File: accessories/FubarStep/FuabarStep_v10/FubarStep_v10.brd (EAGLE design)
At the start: 71.1 x 85.7 mm, 10 parts, among them IC1 7805, X1 DC21MMX

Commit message: More work.
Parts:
- removed AD: (no value), pinhead:1X06
- removed IOL, POWER: (no value), pinhead:1X08
- added C10, C11, C12, C13, C14, C15, C18, C19, C8, C9: .1uF, SparkFun-Capacitors:CAP-PTH-SMALL
- added C16, C17, C5: 100uF, SparkFun-Capacitors:CPOL-RADIAL-100UF-25V
- added IC2, IC3: SN754410NE, texas:DIL16
- added JP10, JP11, JP12, JP13, JP14, JP15, JP16, JP17, JP18, JP19, JP20, JP21, JP22, JP23, JP24, JP25, JP26, JP27, JP3, JP4, JP5, JP6: (no value), SparkFun-Connectors:1X03_LOCK
- added JP2: (no value), SparkFun-Connectors:SCREWTERMINAL-3.5MM-4_LOCK
- added JP7, JP8, JP9: (no value), SparkFun-Connectors:1X04_LOCK
- added LOGO1: OSHW-LOGOM, SparkFun-Aesthetics:OSHW-LOGO-M
- C2: value 10uF -> 100uF; device SparkFun-Capacitors:CPOL-RADIAL-10UF-25V -> SparkFun-Capacitors:CPOL-RADIAL-100UF-25V
- IC1: value 7805 -> OKI-78SR-5/1.5-W36H-C
- JP1: device pinhead:1X10 -> SparkFun-Connectors:SCREWTERMINAL-3.5MM-4_LOCK
- moved JP1 47.7 mm to (47.6, 6.35), turned to 0 degrees
- moved C1 32.2 mm to (27.9, 44.5), turned to 180 degrees
- moved C2 28.7 mm to (17.8, 43.8), turned to 180 degrees
- moved X1 14.2 mm to (19.6, 9.14), turned to 180 degrees
- moved IC1 10.0 mm to (15.2, 35.6), turned to 90 degrees
- moved U$1 6.98 mm to (35.6, 61.0)
- moved U$2 6.98 mm to (25.4, 61.0)
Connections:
- removed net AD0: AD.1
- removed net AD1: AD.2
- removed net AD2: AD.3
- removed net AD3: AD.4
- removed net AD4: AD.5
- removed net AD4/SDA: JP1.9
- removed net AD5: AD.6
- removed net AD5/SCL: JP1.10
- removed net AREF: JP1.8
- removed net IO0: IOL.1
- removed net IO1: IOL.2
- removed net IO2: IOL.3
- removed net IO3: IOL.4
- removed net IO4: IOL.5
- removed net IO5: IOL.6
- removed net IO6: IOL.7
- removed net IO7: IOL.8
- removed net IO8: JP1.1
- removed net IO9: JP1.2
- removed net MISO: JP1.5
- removed net MOSI: JP1.4
- removed net SCK: JP1.6
- removed net SS: JP1.3
- new net M1A1: IC2.2
- new net M1A2: IC2.7
- new net M1A3: IC2.10
- new net M1A4: IC2.15
- new net M1EN12: IC2.1, U$1.11
- new net M1EN34: IC2.9, U$1.12
- new net M1O1: C10.2, IC2.3, JP1.1
- new net M1O2: C11.2, IC2.6, JP1.2
- new net M1O3: C12.1, IC2.11, JP1.3
- new net M1O4: C9.1, IC2.14, JP1.4
- new net M2A1: IC3.2
- new net M2A2: IC3.7
- new net M2A3: IC3.10
- new net M2A4: IC3.15
- new net M2EN12: IC3.1, U$1.13
- new net M2EN34: IC3.9, U$1.14
- new net M2O1: C8.2, IC3.3, JP2.1
- new net M2O2: C13.2, IC3.6, JP2.2
- new net M2O3: C15.1, IC3.11, JP2.3
- new net M2O4: C14.1, IC3.14, JP2.4
- new net N$12: JP8.1
- new net N$2: JP18.1
- new net N$29: JP9.1
- new net N$3: JP19.1
- new net N$67: JP9.2
- new net N$68: JP9.3
- new net N$69: JP23.1
- new net N$87: JP22.1
- new net N$88: JP17.1
- new net N$89: JP16.1
- new net N$90: JP15.1
- new net N$91: JP14.1
- new net N$92: JP10.1
- new net N$93: JP11.1
- new net N$94: JP12.1
- new net N$95: JP13.1
- new net N$96: JP24.1
- new net N$97: JP25.1
- new net RX: JP7.3, U$1.52
- new net SERVO1: JP6.1
- new net SERVO2: JP3.1
- new net SERVO3: JP4.1
- new net SERVO4: JP5.1
- new net TX: JP7.2, U$1.53
- net +3V3: no longer POWER.4
- net +5V: now also C18.1, C19.1, C5.1, IC2.16, IC3.16, JP10.2, JP11.2, JP12.2, JP13.2, JP14.2, JP15.2, JP16.2, JP17.2, JP18.2, JP19.2, JP20.2, JP21.2, JP22.2, JP23.2, JP24.2, JP25.2, JP26.2, JP27.2, JP3.2, JP4.2, JP5.2, JP6.2, JP7.1, U$1.56, U$2.40; no longer POWER.2, POWER.5, U$1.1, U$2.1
- net GND: now also C10.1, C11.1, C12.2, C13.1, C14.2, C15.2, C16.2, C17.2, C18.2, C19.2, C5.2, C8.1, C9.2, IC2.12, IC2.13, IC2.4, IC2.5, IC3.12, IC3.13, IC3.4, IC3.5, JP10.3, JP11.3, JP12.3, JP13.3, JP14.3, JP15.3, JP16.3, JP17.3, JP18.3, JP19.3, JP20.3, JP21.3, JP22.3, JP23.3, JP24.3, JP25.3, JP26.3, JP27.3, JP3.3, JP4.3, JP5.3, JP6.3, JP7.4, JP8.4, JP9.4; no longer JP1.7, POWER.6, POWER.7
- net N$11: now also JP20.1; no longer U$1.11
- net N$13: now also JP8.2; no longer U$1.12
- net N$14: now also JP8.3; no longer U$1.13
- net N$15: now also JP21.1; no longer U$1.14
- net N$33: now also JP26.1; no longer U$1.53
- net N$34: now also JP27.1; no longer U$1.52
- net RESET: no longer POWER.3
- net VIN: now also C16.1, C17.1, IC2.8, IC3.8; no longer POWER.8, U$1.56, U$2.40
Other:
- board size 71.1 x 85.7 mm -> 71.1 x 83.8 mm
- board text removed: "#"
- board text removed: "0"
- board text removed: "1"
- board text removed: "10"
- board text removed: "11"
- board text removed: "12"
- board text removed: "13"
- board text removed: "2"
- board text removed: "3"
- board text removed: "3V3"
- board text removed: "4"
- board text removed: "5"
- board text removed: "5V"
- board text removed: "6"
- board text removed: "7"
- board text removed: "8"
- board text removed: "9"
- board text removed: "A0"
- board text removed: "A1"
- board text removed: "A2"
- board text removed: "A3"
- board text removed: "A4"
- board text removed: "A5"
- board text removed: "ANALOG IN"
- board text removed: "AREF"
- board text removed: "DIGITAL"
- board text removed: "GND"
- board text removed: "RESET"
- board text removed: "RX"
- board text removed: "TX"
- board text removed: "VIN"
- board text removed: "[#=PWM]"

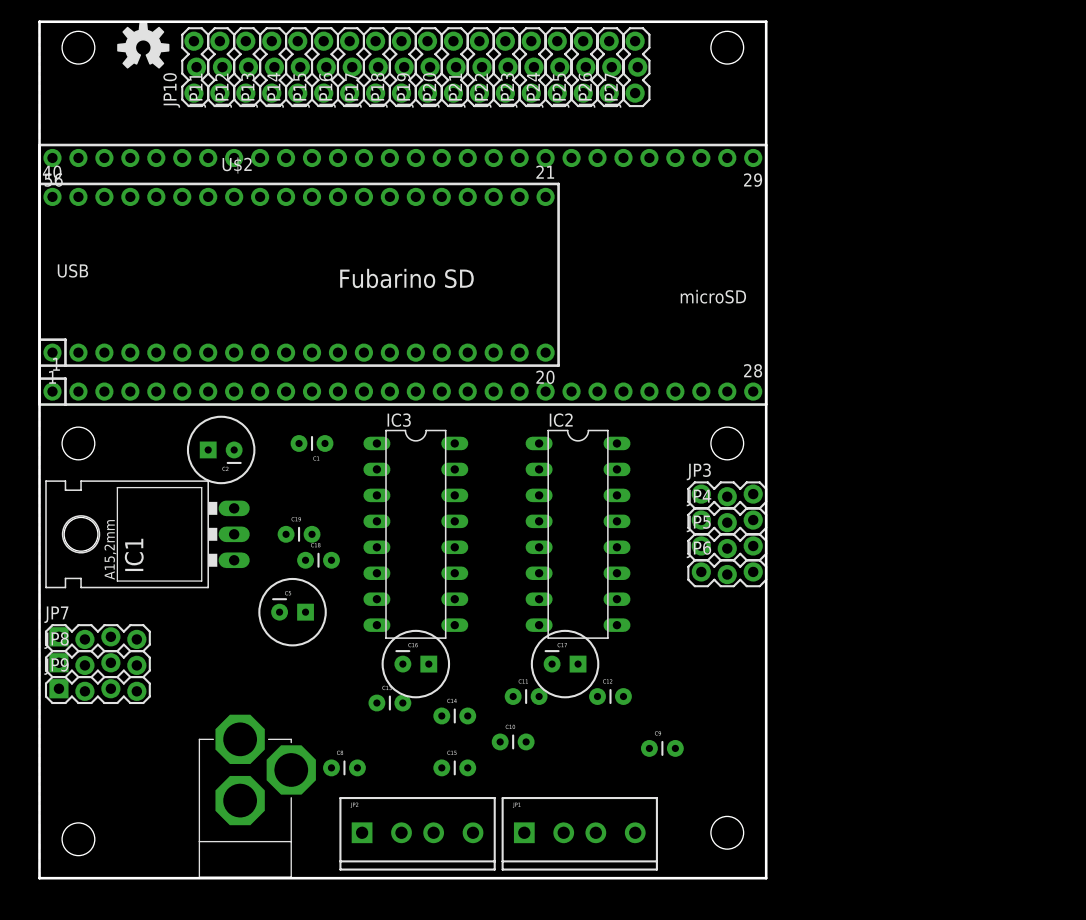
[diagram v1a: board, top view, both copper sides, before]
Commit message: Renamed board from thin to normal, added all Mini routing except for 2 pins (maybe TX/RX?) Almost done!
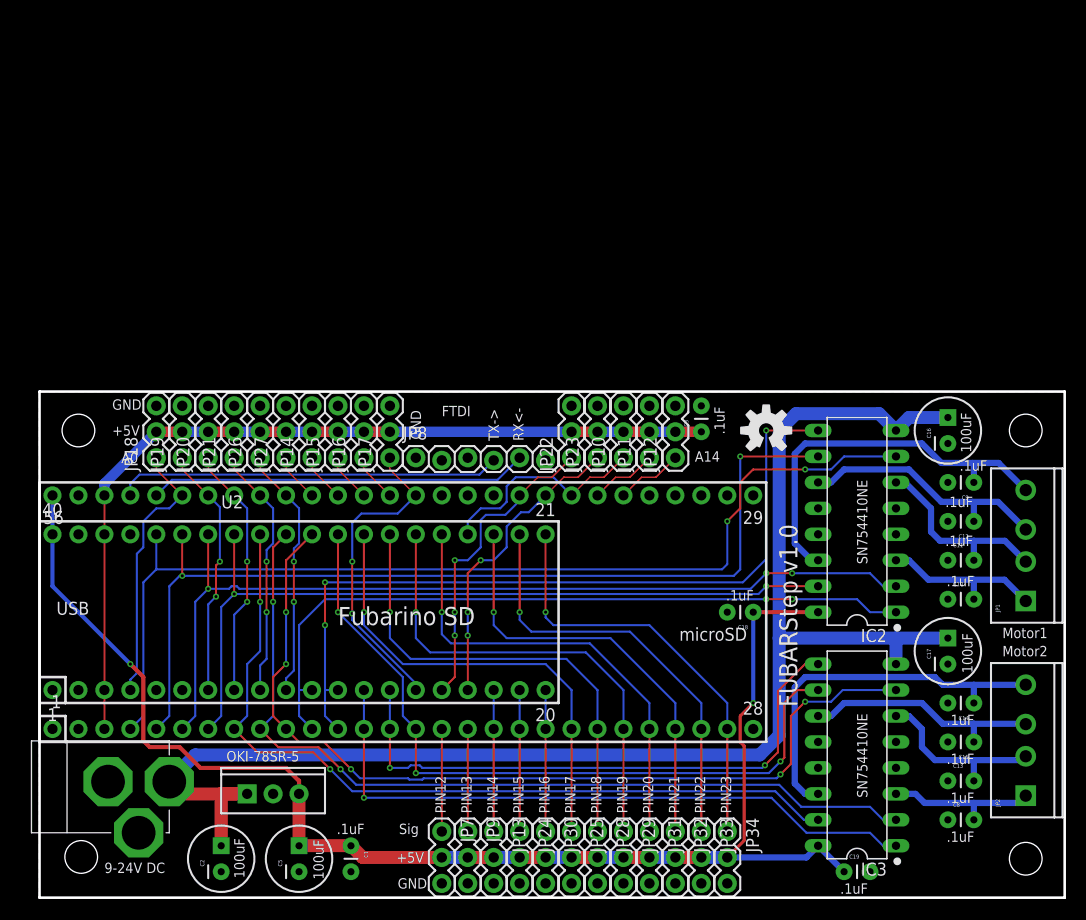
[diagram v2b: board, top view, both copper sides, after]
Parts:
- removed IC1: OKI-78SR-5/1.5-W36H-C, SparkFun-PowerIC:78XXL
- removed JP3, JP4, JP5, JP6: (no value), SparkFun-Connectors:1X03_LOCK
- removed U$1: FUBARINO_SD, SchmalzHausPublic:FUBARINO_SD
- removed U$2: FUBARINO_MINI, SchmalzHausPublic:FUBARINO_MINI
- added C3: .1uF, SparkFun-Capacitors:CAP-PTH-SMALL
- added JP28, JP29, JP30, JP31, JP32, JP33, JP34: (no value), SparkFun-Connectors:1X03
- added U1: FUBARINO_SD, SchmalzHausPublic:FUBARINO_SD
- added U2: FUBARINO_MINI, SchmalzHausPublic:FUBARINO_MINI
- added U3: OKI-78SR-5/1.5-W36H-C, SparkFun-PowerIC:TO220-IGO
- JP10, JP11, JP12, JP13, JP14, JP15, JP16, JP17, JP18, JP19, JP20, JP21, JP22, JP23, JP24, JP25, JP26, JP27: device SparkFun-Connectors:1X03_LOCK -> SparkFun-Connectors:1X03
- JP7, JP9: device SparkFun-Connectors:1X04_LOCK -> SparkFun-Connectors:1X03
- JP8: device SparkFun-Connectors:1X04_LOCK -> SparkFun-Connectors:1X06_LOCK
- moved JP13 75.4 mm to (44.5, 6.48), turned to 270 degrees
- moved JP24 72.4 mm to (47.0, 6.48), turned to 270 degrees
- moved JP25 72.3 mm to (52.1, 6.48), turned to 270 degrees
- moved LOGO1 71.6 mm to (71.1, 45.7)
- moved JP2 64.9 mm to (96.5, 10.2), turned to 90 degrees
- moved C19 63.8 mm to (78.7, 2.54)
- moved C8 60.5 mm to (88.9, 7.62)
- moved C16 56.9 mm to (88.9, 45.7), turned to 90 degrees
- moved C13 56.4 mm to (88.9, 11.4)
- moved JP10 55.0 mm to (57.1, 43.1)
- moved JP11 55.0 mm to (59.7, 43.1)
- moved JP12 55.0 mm to (62.2, 43.1)
- moved JP1 54.0 mm to (96.5, 29.2), turned to 90 degrees
- moved C15 52.1 mm to (91.4, 15.2), turned to 180 degrees
- moved C14 52.1 mm to (91.4, 19.1), turned to 180 degrees
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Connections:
- removed net N$10: U$1.10
- removed net N$11: JP20.1
- removed net N$12: JP8.1
- removed net N$13: JP8.2
- removed net N$14: JP8.3
- removed net N$15: JP21.1
- removed net N$16: U$1.15
- removed net N$17: U$1.16
- removed net N$18: U$1.17
- removed net N$19: U$1.18
- removed net N$2: JP18.1
- removed net N$20: U$1.19
- removed net N$21: U$1.20
- removed net N$22: U$1.21
- removed net N$23: U$1.22
- removed net N$24: U$1.23
- removed net N$25: U$1.24
- removed net N$26: U$1.25
- removed net N$27: U$1.26
- removed net N$28: U$1.27
- removed net N$29: JP9.1
- removed net N$3: JP19.1
- removed net N$30: U$2.36
- removed net N$31: U$2.35
- removed net N$32: U$2.34
- removed net N$33: JP26.1
- removed net N$34: JP27.1
- removed net N$35: U$1.51
- removed net N$36: U$1.50
- removed net N$37: U$1.49
- removed net N$38: U$1.48
- removed net N$39: U$1.47
- removed net N$4: U$1.4
- removed net N$40: U$1.46
- removed net N$41: U$1.45
- removed net N$42: U$1.44
- removed net N$43: U$1.43
- removed net N$44: U$1.42
- removed net N$45: U$2.33
- removed net N$46: U$2.32
- removed net N$47: U$2.31
- removed net N$48: U$1.38
- removed net N$49: U$1.37
- removed net N$5: U$1.5
- removed net N$50: U$1.36
- removed net N$51: U$1.35
- removed net N$52: U$1.34
- removed net N$53: U$1.33
- removed net N$54: U$1.32
- removed net N$55: U$1.31
- removed net N$56: U$1.30
- removed net N$57: U$2.30
- removed net N$58: U$2.29
- removed net N$59: U$2.28
- removed net N$6: U$1.6
- removed net N$60: U$2.27
- removed net N$61: U$2.26
- removed net N$62: U$2.25
- removed net N$63: U$2.24
- removed net N$64: U$2.23
- removed net N$65: U$2.22
- removed net N$66: U$2.21
- removed net N$67: JP9.2
- removed net N$68: JP9.3
- removed net N$69: JP23.1
- removed net N$7: U$1.7
- removed net N$70: U$2.4
- removed net N$71: U$2.5
- removed net N$72: U$2.6
- removed net N$73: U$2.7
- removed net N$74: U$2.8
- removed net N$75: U$2.9
- removed net N$76: U$2.10
- removed net N$77: U$2.11
- removed net N$78: U$2.12
- removed net N$79: U$2.13
- removed net N$8: U$1.8
- removed net N$80: U$2.14
- removed net N$81: U$2.15
- removed net N$82: U$2.16
- removed net N$83: U$2.17
- removed net N$84: U$2.18
- removed net N$85: U$2.19
- removed net N$86: U$2.20
- removed net N$87: JP22.1
- removed net N$88: JP17.1
- removed net N$89: JP16.1
- removed net N$9: U$1.9
- removed net N$90: JP15.1
- removed net N$91: JP14.1
- removed net N$92: JP10.1
- removed net N$93: JP11.1
- removed net N$94: JP12.1
- removed net N$95: JP13.1
- removed net N$96: JP24.1
- removed net N$97: JP25.1
- removed net SERVO1: JP6.1
- removed net SERVO2: JP3.1
- removed net SERVO3: JP4.1
- removed net SERVO4: JP5.1
- new net $01: U2.5
- new net $02: U2.6
- new net 3.3V: C3.1, JP10.2, JP11.2, JP12.2, JP14.2, JP15.2, JP16.2, JP17.2, JP18.2, JP19.2, JP20.2, JP21.2, JP22.2, JP23.2, JP26.2, JP27.2, U1.3, U1.54, U2.3, U2.38
- new net A0: JP18.1, U1.51, U2.4
- new net A1: JP19.1, U1.50, U2.7
- new net A10: JP22.1, U1.38, U2.16
- new net A11: JP23.1, U1.37, U2.17
- new net A12: JP10.1, U1.36, U2.24
- new net A13: JP11.1, U1.35
- new net A14: JP12.1, U1.34
- new net A2: JP20.1, U1.49, U2.8
- new net A3: JP21.1, U1.48, U2.9
- new net A4: JP26.1, U1.47, U2.10
- new net A5: JP27.1, U1.46
- new net A6: JP14.1, U1.45
- new net A7: JP15.1, U1.44
- new net A8: JP16.1, U1.43
- new net A9: JP17.1, U1.42, U2.15
- new net PIN12: JP7.1, U1.16
- new net PIN13: JP9.1, U1.17
- new net PIN14: JP13.1, U1.18, U2.18
- new net PIN15: JP24.1, U1.19, U2.19
- new net PIN16: JP30.1, U1.20, U2.20
- new net PIN17: JP25.1, U1.21, U2.28
- new net PIN18: JP28.1, U1.22, U2.27
- new net PIN19: JP29.1, U1.23, U2.26
- new net PIN20: JP31.1, U1.24, U2.25
- new net PIN21: JP32.1, U1.25, U2.23
- new net PIN22: JP33.1, U1.26, U2.22
- new net PIN23: JP34.1, U1.27, U2.21
- net +3V3: now also U1.40; no longer U$1.3, U$1.40, U$1.54, U$2.3, U$2.38
- net +5V: now also JP28.2, JP29.2, JP30.2, JP31.2, JP32.2, JP33.2, JP34.2, JP7.2, JP9.2, U1.56, U2.40, U3.OUT; no longer IC1.OUT, JP10.2, JP11.2, JP12.2, JP14.2, JP15.2, JP16.2, JP17.2, JP18.2, JP19.2, JP20.2, JP21.2, JP22.2, JP23.2, JP26.2, JP27.2, JP3.2, JP4.2, JP5.2, JP6.2, JP7.1, U$1.56, U$2.40
- net GND: now also C3.2, JP28.3, JP29.3, JP30.3, JP31.3, JP32.3, JP33.3, JP34.3, JP7.3, JP8.1, JP9.3, U1.2, U1.28, U1.29, U1.41, U1.55, U2.2, U2.37, U2.39, U3.GND; no longer IC1.GND, JP3.3, JP4.3, JP5.3, JP6.3, JP7.4, JP8.4, JP9.4, U$1.2, U$1.28, U$1.29, U$1.41, U$1.55, U$2.2, U$2.37, U$2.39
- net M1A1: now also U1.6, U2.34
- net M1A2: now also U1.4, U2.36
- net M1A3: now also U1.5, U2.35
- net M1A4: now also U1.7, U2.33
- net M1EN12: now also U1.11, U2.11; no longer U$1.11
- net M1EN34: now also U1.12, U2.12; no longer U$1.12
- net M2A1: now also U1.9, U2.31
- net M2A2: now also U1.10, U2.30
- net M2A3: now also U1.15, U2.29
- net M2A4: now also U1.8, U2.32
- net M2EN12: now also U1.13, U2.13; no longer U$1.13
- net M2EN34: now also U1.14, U2.14; no longer U$1.14
- net RESET: now also U1.39; no longer U$1.39
- net RX: now also JP8.5, U1.52; no longer JP7.3, U$1.52
- net TX: now also JP8.4, U1.53; no longer JP7.2, U$1.53
- net VIN: now also U3.IN; no longer IC1.IN
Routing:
- net VIN: track 0.00 -> 144.6 mm
- net +5V: track 0.00 -> 138.0 mm, vias 0 -> 2
- net M1A2: track 0.00 -> 101.0 mm, vias 0 -> 2
- net M1A3: track 0.00 -> 93.8 mm, vias 0 -> 2
- net M2A2: track 0.00 -> 89.3 mm, vias 0 -> 5
- net M1A1: track 0.00 -> 88.8 mm, vias 0 -> 3
- net M2A1: track 0.00 -> 86.0 mm, vias 0 -> 2
- net 3.3V: track 0.00 -> 84.5 mm
- net M2A4: track 0.00 -> 80.9 mm, vias 0 -> 2
- net M1EN34: track 0.00 -> 77.9 mm, vias 0 -> 3
- net M1A4: track 0.00 -> 77.6 mm, vias 0 -> 2
- net M2A3: track 0.00 -> 72.4 mm, vias 0 -> 3
- net M1EN12: track 0.00 -> 72.0 mm, vias 0 -> 2
- net M2EN12: track 0.00 -> 64.6 mm, vias 0 -> 1
- net M2EN34: track 0.00 -> 57.4 mm, vias 0 -> 2
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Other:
- board size 71.1 x 83.8 mm -> 100.3 x 49.5 mm
- board text added: "+5V"
- board text added: ".1uF"
- board text added: "100uF"
- board text added: "9-24V DC"
- board text added: "A0"
- board text added: "A14"
- board text added: "ANALOG INPUTS/3.3V GPIO"
- board text added: "FTDI"
- board text added: "FUBARStep v1.0"
- board text added: "GND"
- board text added: "Motor1"
- board text added: "Motor2"
- board text added: "OKI-78SR-5"
- board text added: "PIN12"
- board text added: "PIN13"
- board text added: "PIN14"
- board text added: "PIN15"
- board text added: "PIN16"
- board text added: "PIN17"
- board text added: "PIN18"
- board text added: "PIN19"
- board text added: "PIN20"
- board text added: "PIN21"
- board text added: "PIN22"
- board text added: "PIN23"
- board text added: "RX<-"
- board text added: "SERVO OUTPUTS/5V GPIO"
- board text added: "SN754410NE"
- board text added: "Sig"
- board text added: "TX->"

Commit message: Version 1.0 done - routed, schematic done (with license), just need to add BOM now.
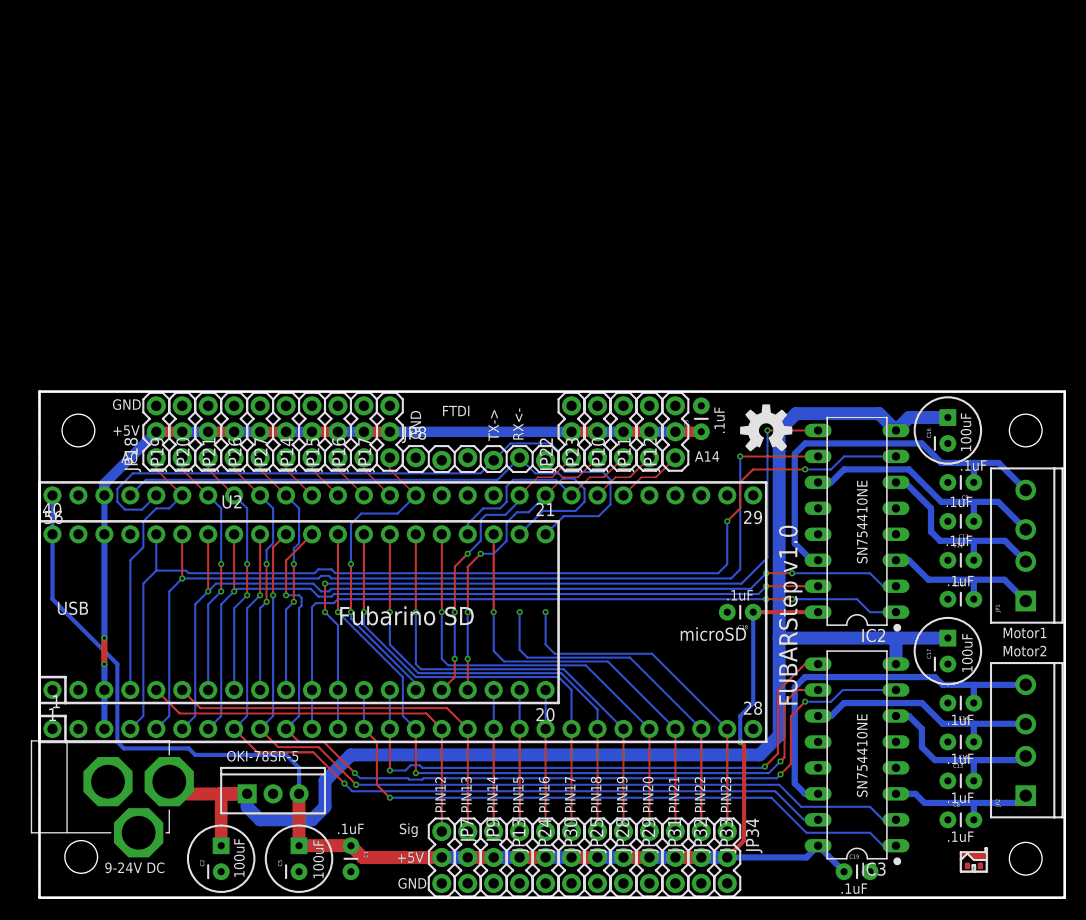
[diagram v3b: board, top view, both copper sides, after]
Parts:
- added U$1: SCHMALZHAUSSCHMALZHAUS_SMALL, SchmalzHaus:SCHMALZHAUS_SMALL
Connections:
- removed net $01: U2.5
- removed net $02: U2.6
- net PIN12: now also U2.5
- net PIN13: now also U2.6
- net PIN22: no longer U2.22
- net PIN23: no longer U2.21
- net RX: now also JP8.4, U2.21; no longer JP8.5
- net TX: now also JP8.5, U2.22; no longer JP8.4
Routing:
- net RX: track 37.1 -> 68.3 mm
- net PIN13: track 10.0 -> 39.6 mm
- net PIN12: track 10.0 -> 39.6 mm
- net TX: track 37.6 -> 56.2 mm
- net PIN23: track 42.0 -> 34.4 mm
- net PIN22: track 42.1 -> 34.7 mm
- net VIN: track 144.6 -> 141.9 mm
- net +5V: track 138.0 -> 140.3 mm, vias 2 -> 1
- net M1EN12: track 72.0 -> 69.9 mm
- net M2EN12: track 64.6 -> 63.1 mm
- net M1EN34: track 77.9 -> 76.5 mm
- net M2A2: track 89.3 -> 90.2 mm, vias 5 -> 4
- net PIN18: track 46.4 -> 45.7 mm
- net PIN19: track 46.4 -> 45.7 mm
- net A10: track 30.7 -> 29.9 mm
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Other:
- board text added: "FUBARStep v1.0 Creatded by FUBARLabs and Schmalz Haus www.fubarlabs.org www.schmalzhaus.com www.fubarino.org"

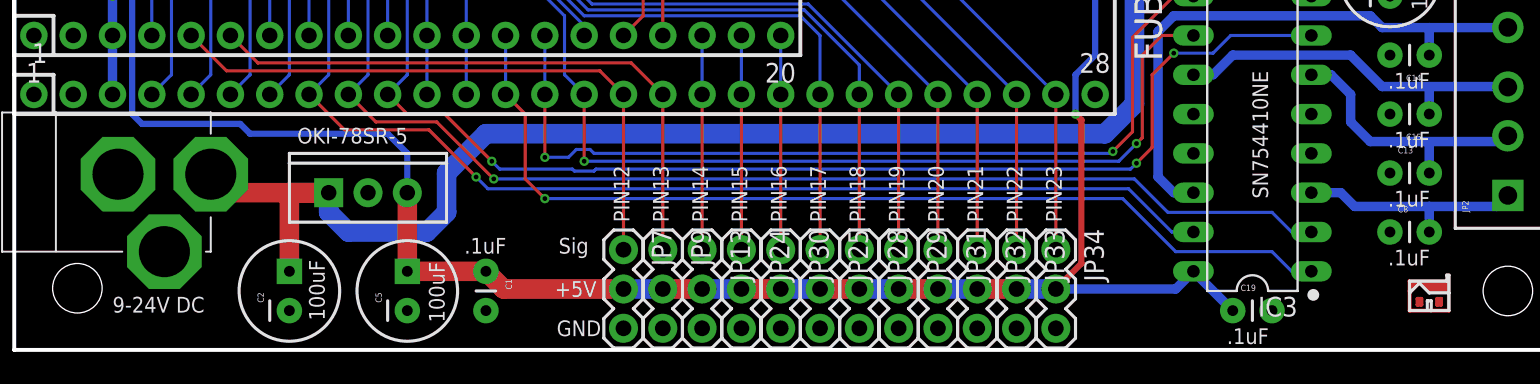
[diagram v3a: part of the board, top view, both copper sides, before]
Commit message: Added power mode jumper to select between 12V and 5V inputs. Added two ground pins for debugging Added 2-pin screw terminal for extra power input option.
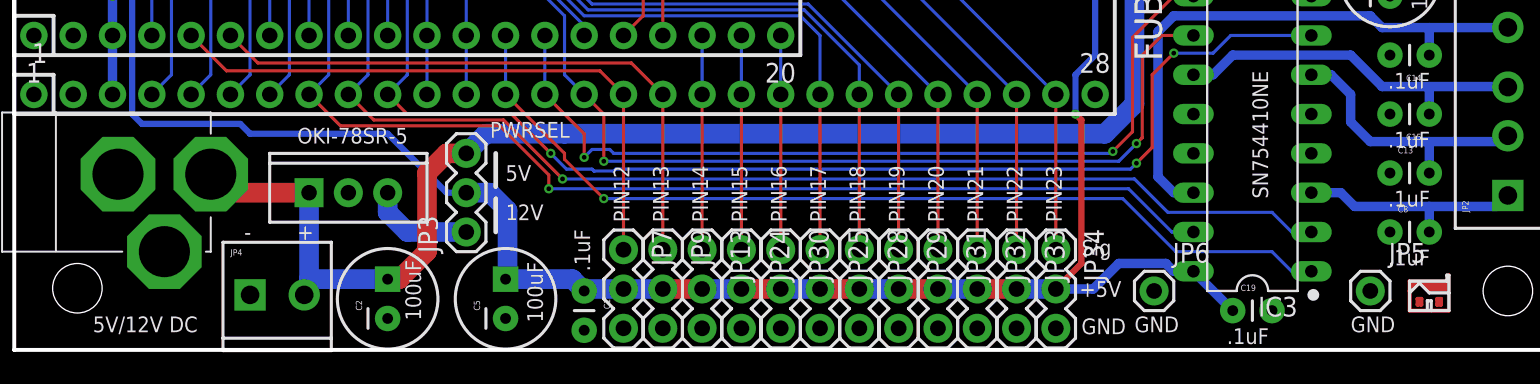
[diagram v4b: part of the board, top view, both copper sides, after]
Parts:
- added JP3: (no value), SparkFun-Connectors:1X03
- added JP4: (no value), SparkFun-Connectors:SCREWTERMINAL-3.5MM-2
- added JP5, JP6: M01PTH, SparkFun-Connectors:1X01
- moved C1 6.48 mm to (36.8, 3.81)
- moved C5 6.37 mm to (31.8, 3.30)
- moved C2 6.37 mm to (24.1, 3.30)
- moved U3 1.27 mm to (21.6, 10.2)
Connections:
- new net N$2: JP3.1, U3.OUT
- net +5V: now also JP3.2; no longer U3.OUT
- net GND: now also JP4.1, JP5.1, JP6.1
- net VIN: now also JP3.3, JP4.2
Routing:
- net N$2: track 0.00 -> 6.88 mm
- net M2EN12: track 63.1 -> 60.8 mm
- net M2EN34: track 57.9 -> 56.4 mm
- net +5V: track 140.3 -> 139.1 mm
- net M2A3: track 72.4 -> 71.6 mm
- net M2A4: track 80.9 -> 81.5 mm
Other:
- board text added: "+"
- board text added: "-"
- board text added: "12V"
- board text added: "5V"
- board text added: "5V/12V DC"
- board text added: "PWRSEL"
- board text removed: "9-24V DC"
